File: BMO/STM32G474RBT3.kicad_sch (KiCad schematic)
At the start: 34 parts, among them J1 EXT, J2 Conn_ST_STDC14, SW1 USER, SW2 SW_Push, U1 STM32G474RBTx, Y1 16MHz

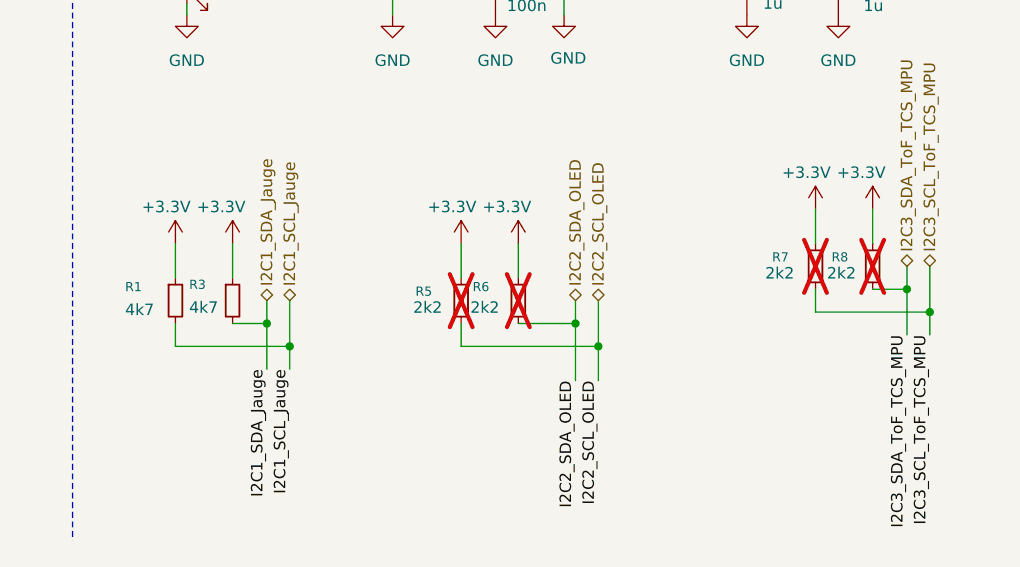
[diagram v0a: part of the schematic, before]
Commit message: feat(pcb): complete initial routing (v1) pending verification
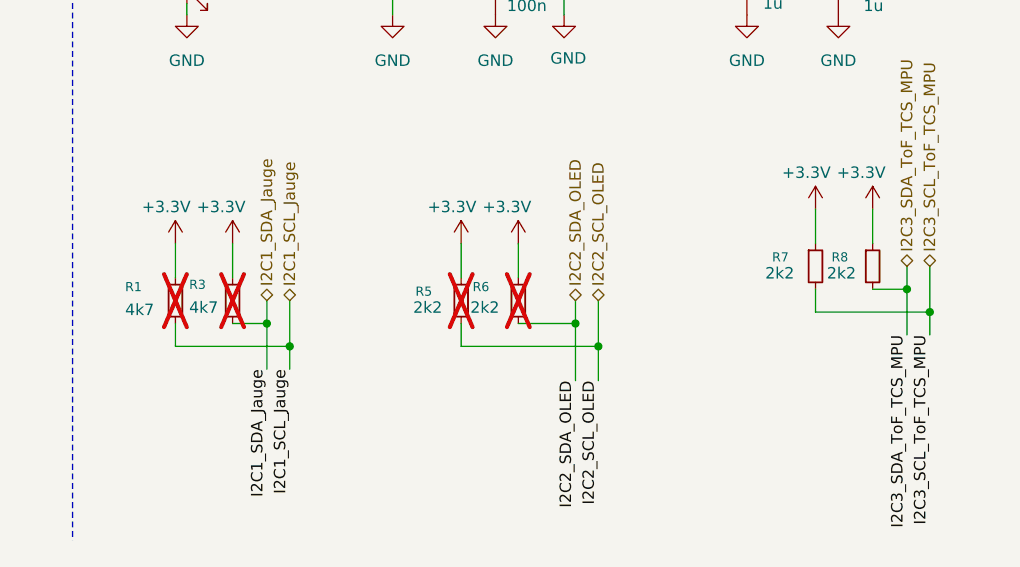
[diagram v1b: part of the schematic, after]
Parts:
- R1, R3: now not fitted
- R7, R8: now fitted

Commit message: Finalize PCB design and generate BOM and CPL files
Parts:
- R1, R3: now fitted
- renumbered TP10 to 3V3A1, C9 to C10, C10 to C11, C11 to C12, C12 to C13, C45 to C4, C4 to C5, C5 to C6, C6 to C7, C7 to C8, C8 to C9
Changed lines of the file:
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@@
 		(in_pos_files yes)
 		(dnp no)
-		(property "Reference" "C10"
+		(property "Reference" "C11"
 			(at 231.902 102.87 0)
 			(show_name no)
@@
 			(project "BMO"
 				(path "/509804e7-65e7-46e6-80ed-6cdb4037dc07/6ae9c4a4-c173-43ed-93f8-54a31d5275c1"
-					(reference "C10")
+					(reference "C11")
 					(unit 1)
 				)
@@
 		(dnp no)
 		(fields_autoplaced yes)
-		(property "Reference" "C8"
+		(property "Reference" "C9"
 			(at 88.9 34.2835 0)
 			(show_name no)
@@
 			(project "BMO"
 				(path "/509804e7-65e7-46e6-80ed-6cdb4037dc07/6ae9c4a4-c173-43ed-93f8-54a31d5275c1"
-					(reference "C8")
+					(reference "C9")
 					(unit 1)
 				)
@@
 		(dnp no)
 		(fields_autoplaced yes)
-		(property "Reference" "C5"
+		(property "Reference" "C6"
 			(at 64.77 34.2835 0)
 			(show_name no)
@@
 			(project "BMO"
 				(path "/509804e7-65e7-46e6-80ed-6cdb4037dc07/6ae9c4a4-c173-43ed-93f8-54a31d5275c1"
-					(reference "C5")
+					(reference "C6")
 					(unit 1)
 				)
@@
 		(dnp no)
 		(fields_autoplaced yes)
-		(property "Reference" "C9"
+		(property "Reference" "C10"
 			(at 113.03 34.2835 0)
 			(show_name no)
@@
 			(project "BMO"
 				(path "/509804e7-65e7-46e6-80ed-6cdb4037dc07/6ae9c4a4-c173-43ed-93f8-54a31d5275c1"
-					(reference "C9")
+					(reference "C10")
 					(unit 1)
 				)
@@
 		(on_board yes)
 		(in_pos_files yes)
-		(dnp yes)
+		(dnp no)
 		(property "Reference" "R1"
 			(at 188.722 136.906 0)
@@
 		(dnp no)
 		(fields_autoplaced yes)
-		(property "Reference" "C7"
+		(property "Reference" "C8"
 			(at 81.28 34.2835 0)
 			(show_name no)
@@
 			(project "BMO"
 				(path "/509804e7-65e7-46e6-80ed-6cdb4037dc07/6ae9c4a4-c173-43ed-93f8-54a31d5275c1"
-					(reference "C7")
+					(reference "C8")
 					(unit 1)
 				)
@@
 		(in_pos_files yes)
 		(dnp no)
-		(property "Reference" "C11"
+		(property "Reference" "C12"
 			(at 259.588 102.87 0)
 			(show_name no)
@@
 			(project "BMO"
 				(path "/509804e7-65e7-46e6-80ed-6cdb4037dc07/6ae9c4a4-c173-43ed-93f8-54a31d5275c1"
-					(reference "C11")
+					(reference "C12")
 					(unit 1)
 				)
@@
 		(in_pos_files yes)
 		(dnp no)
-		(property "Reference" "C45"
+		(property "Reference" "C4"
 			(at 48.26 34.2835 0)
 			(show_name no)
@@
 			(project "BMO"
 				(path "/509804e7-65e7-46e6-80ed-6cdb4037dc07/6ae9c4a4-c173-43ed-93f8-54a31d5275c1"
-					(reference "C45")
+					(reference "C4")
 					(unit 1)
 				)
@@
 		(dnp no)
 		(fields_autoplaced yes)
-		(property "Reference" "TP10"
+		(property "Reference" "3V3A1"
 			(at 110.49 27.9399 90)
 			(show_name no)
@@
 			(project "BMO"
 				(path "/509804e7-65e7-46e6-80ed-6cdb4037dc07/6ae9c4a4-c173-43ed-93f8-54a31d5275c1"
-					(reference "TP10")
+					(reference "3V3A1")
 					(unit 1)
 				)
@@
 		(in_pos_files yes)
 		(dnp no)
-		(property "Reference" "C12"
+		(property "Reference" "C13"
 			(at 269.748 102.87 0)
 			(show_name no)
@@
 			(project "BMO"
 				(path "/509804e7-65e7-46e6-80ed-6cdb4037dc07/6ae9c4a4-c173-43ed-93f8-54a31d5275c1"
-					(reference "C12")
+					(reference "C13")
 					(unit 1)
 				)
@@
 		(in_pos_files yes)
 		(dnp no)
-		(property "Reference" "C4"
+		(property "Reference" "C5"
 			(at 55.88 34.2835 0)
 			(show_name no)
@@
 			(project "BMO"
 				(path "/509804e7-65e7-46e6-80ed-6cdb4037dc07/6ae9c4a4-c173-43ed-93f8-54a31d5275c1"
-					(reference "C4")
+					(reference "C5")
 					(unit 1)
 				)
@@
 		(dnp no)
 		(fields_autoplaced yes)
-		(property "Reference" "C6"
+		(property "Reference" "C7"
 			(at 73.66 34.2835 0)
 			(show_name no)
@@
 			(project "BMO"
 				(path "/509804e7-65e7-46e6-80ed-6cdb4037dc07/6ae9c4a4-c173-43ed-93f8-54a31d5275c1"
-					(reference "C6")
+					(reference "C7")
 					(unit 1)
 				)
@@
 		(on_board yes)
 		(in_pos_files yes)
-		(dnp yes)
+		(dnp no)
 		(property "Reference" "R3"
 			(at 195.834 136.652 0)
